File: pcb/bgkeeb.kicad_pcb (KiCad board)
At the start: 2 copper layers, 98.4 x 90.5 mm, 102 parts, among them J1 Pimoroni, SW1 SW_Push, SW11 SW_Push, SW12 SW_Push, SW13 SW_Push, SW14 SW_Push, SW15 SW_Push, SW2 SW_Push, SW21 SW_Push, SW22 SW_Push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

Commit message: updated TRRS order
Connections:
- U3 pad 1: Net-(U3-Pad1) -> GND
- U3 pad 2: data -> GND
- U3 pad 3: GND -> data
- U4 pad 1: Net-(U4-Pad1) -> GND
- U4 pad 2: data -> GND
- U4 pad 3: GND -> data
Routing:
- net GND: track 626.4 -> 632.7 mm, vias 57 -> 58
- net data: track 57.3 -> 63.5 mm, vias 2 -> 4

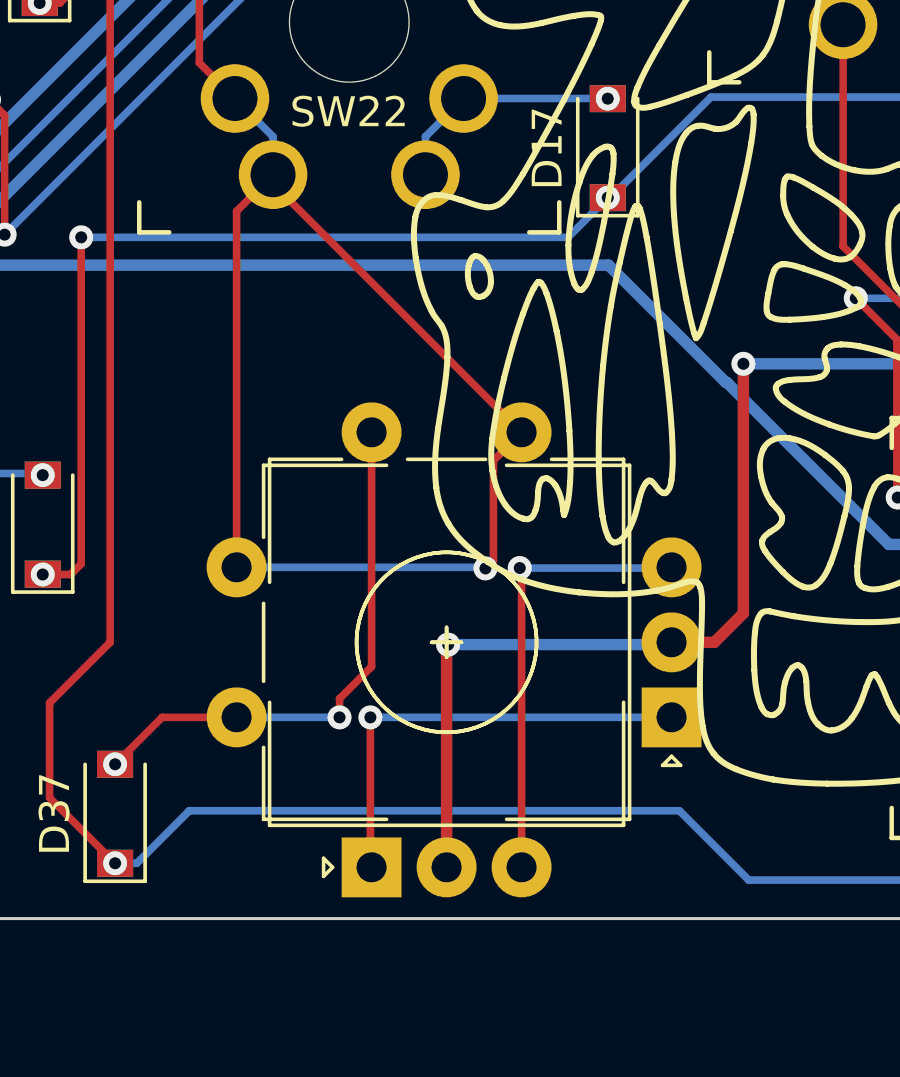
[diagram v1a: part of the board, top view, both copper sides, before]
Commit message: removed old gerber files, fixed rotary encoder on the back
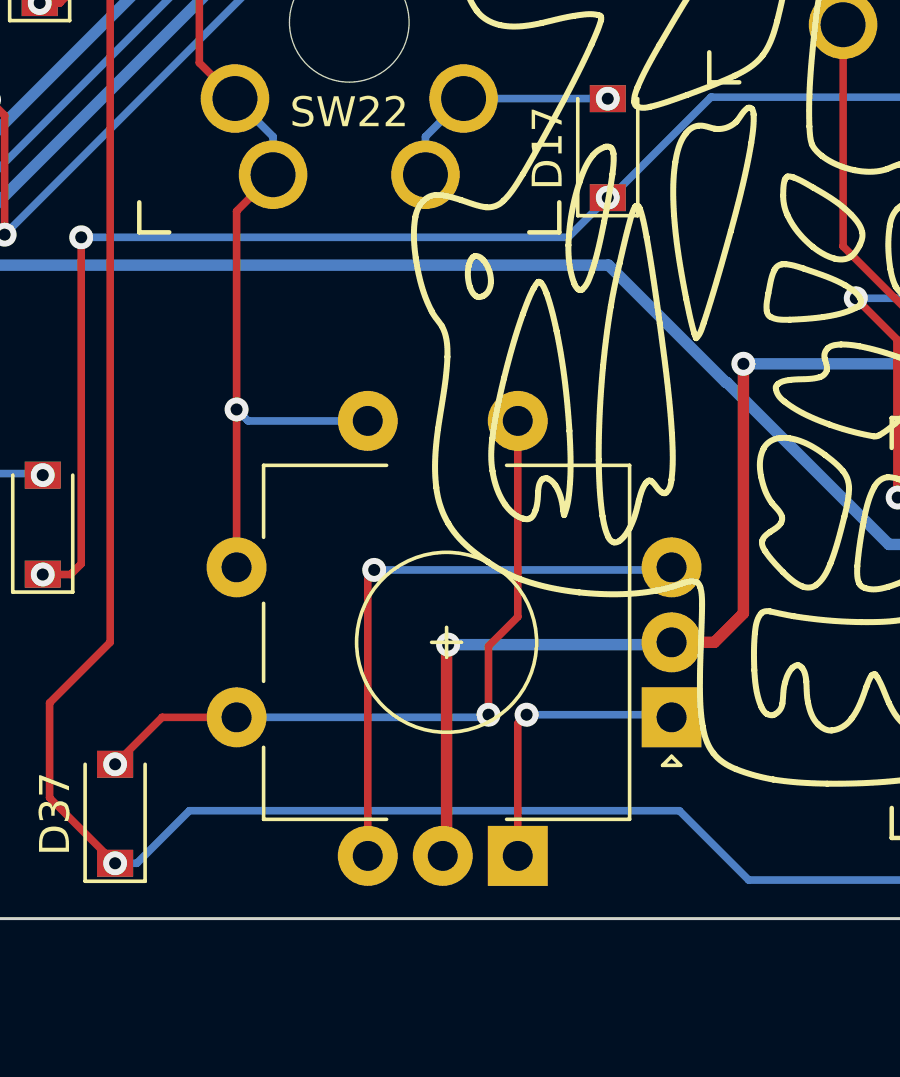
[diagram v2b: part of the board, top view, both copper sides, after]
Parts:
- SW7: moved to B.Cu
- moved SW7 0.40 mm to (83.1, 103.8)
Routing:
- net col1: track 99.6 -> 79.0 mm
- net ENC1A: track 15.1 -> 9.70 mm
- net Net-(D37-Pad2): track 18.1 -> 23.3 mm
- net ENC1B: track 15.1 -> 19.6 mm

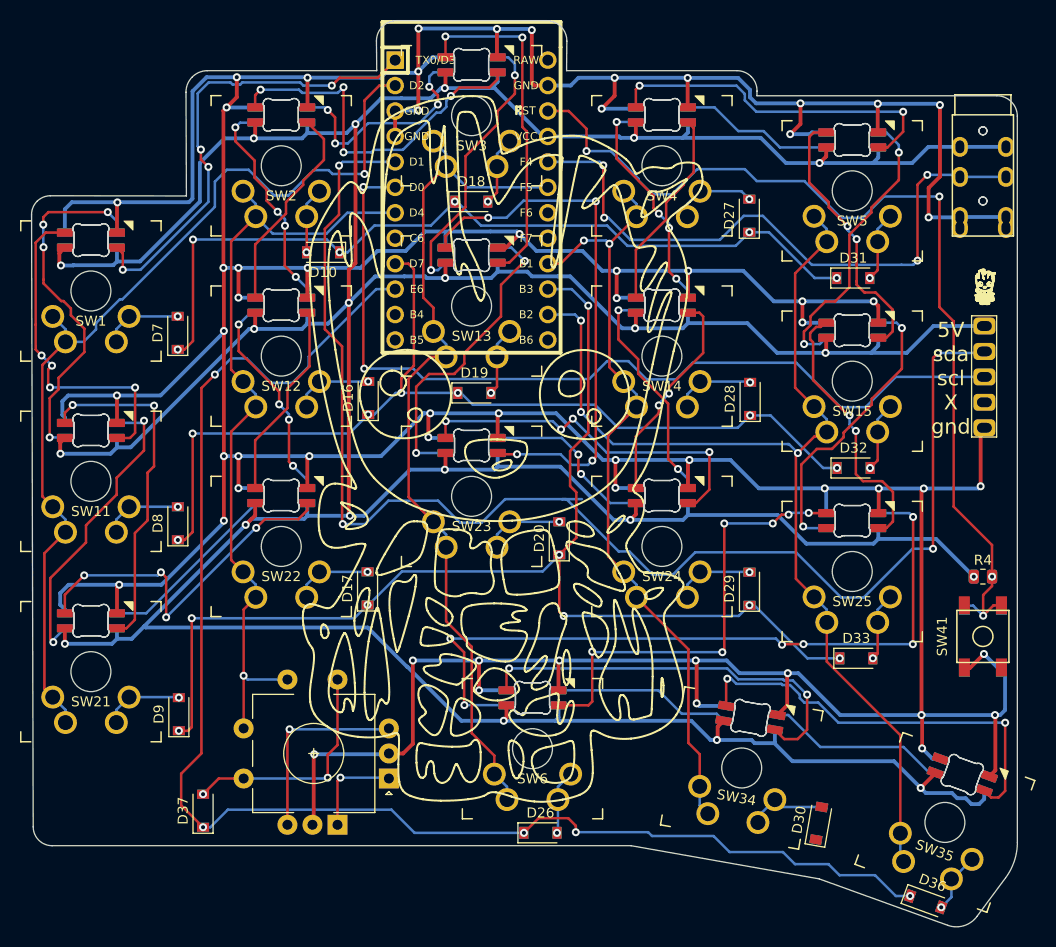
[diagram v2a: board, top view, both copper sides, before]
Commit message: Updated to add mounting holes
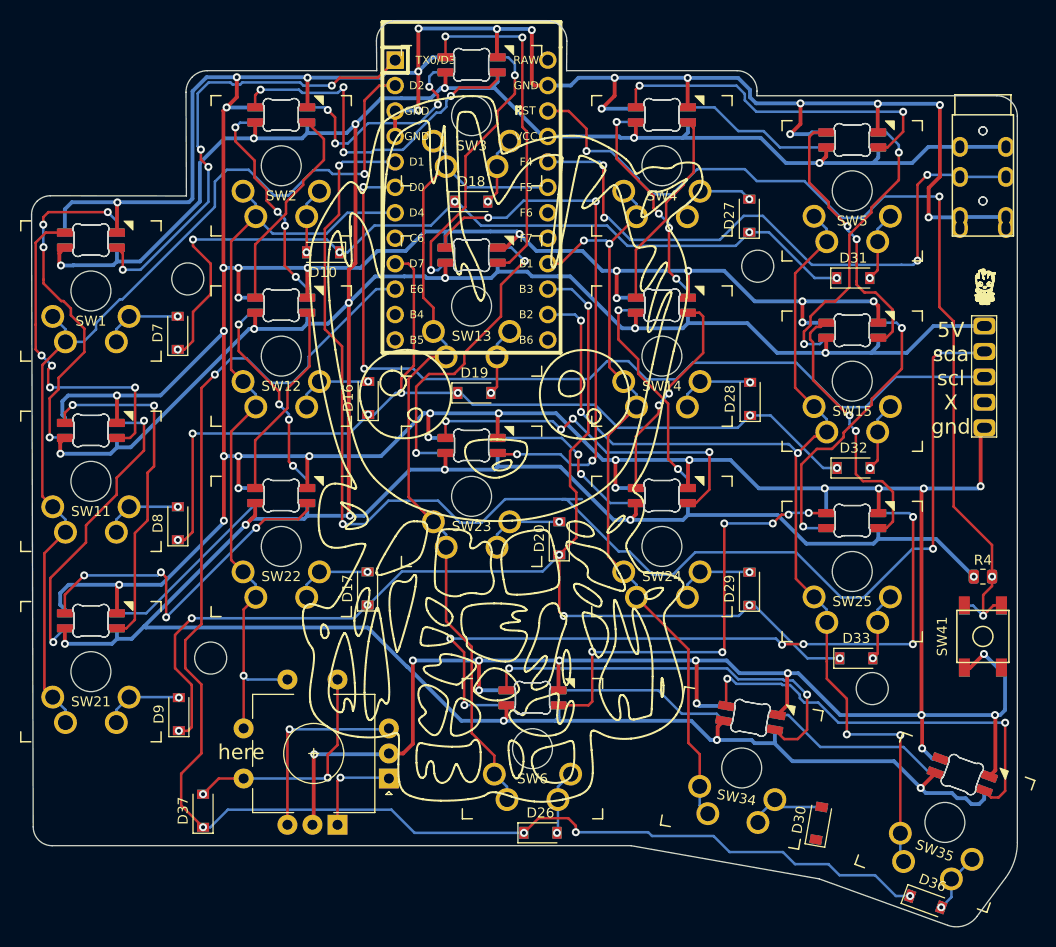
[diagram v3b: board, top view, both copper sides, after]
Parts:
- added ?: MountingHole_3.2mm_M3, MountingHole:MountingHole_3.2mm_M3, F.Cu at (73.0, 94.7)
- added ?: MountingHole_3.2mm_M3, MountingHole:MountingHole_3.2mm_M3, F.Cu at (70.7, 56.8)
- added ?: MountingHole_3.2mm_M3, MountingHole:MountingHole_3.2mm_M3, F.Cu at (127.6, 55.6)
- added ?: MountingHole_3.2mm_M3, MountingHole:MountingHole_3.2mm_M3, F.Cu at (139.0, 97.7)
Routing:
- net col4: track 109.8 -> 112.9 mm, vias 3 -> 5
- net row0: track 83.2 -> 84.6 mm
- net row2: track 119.4 -> 120.8 mm
- net row3: track 148.1 -> 149.4 mm
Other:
- board text added: "here"

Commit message: aux jack wasn't wired, no functional impact, just got DRC errors
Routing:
- net GND: track 632.7 -> 634.9 mm

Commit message: fixed a lot of things
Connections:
- U1 pad 18: Net-(U1-Pad18) -> row0
- U1 pad 2: col0 -> data
- U1 pad 20: data -> col0
- U1 pad 24: row0 -> Net-(U1-Pad24)
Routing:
- net ENC1A: track 9.70 -> 63.0 mm
- net ENC1B: track 19.6 -> 60.7 mm, vias 1 -> 3
- net data: track 63.5 -> 85.1 mm, vias 4 -> 5
- net led: track 46.6 -> 58.5 mm, vias 4 -> 5
- net col0: track 96.8 -> 107.9 mm, vias 1 -> 2
- net row3: track 149.4 -> 152.1 mm, vias 5 -> 6
- net +5V: track 500.7 -> 502.5 mm, vias 21 -> 22
- net row0: track 84.6 -> 85.7 mm
- net Net-(D30-Pad2): vias 0 -> 1

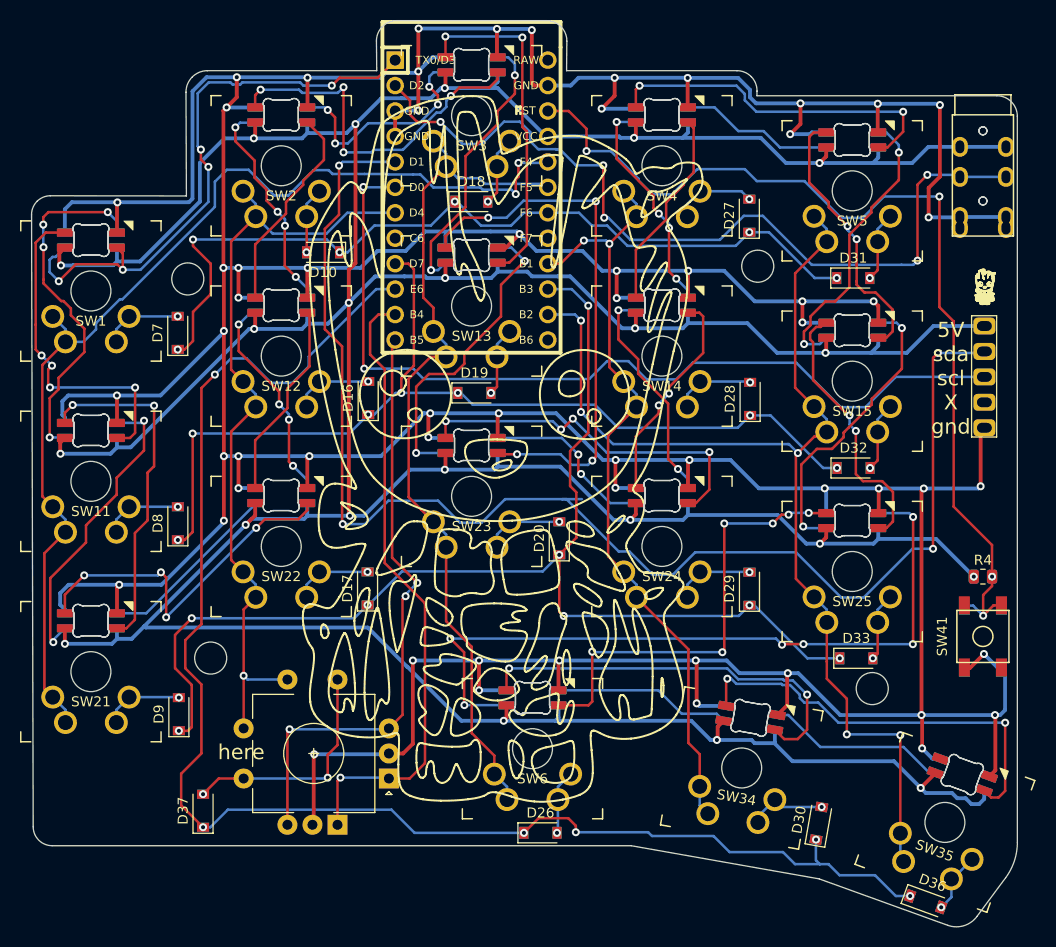
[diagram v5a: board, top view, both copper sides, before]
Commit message: v2 fixes the diode direction being flipped on the reverse side of the board
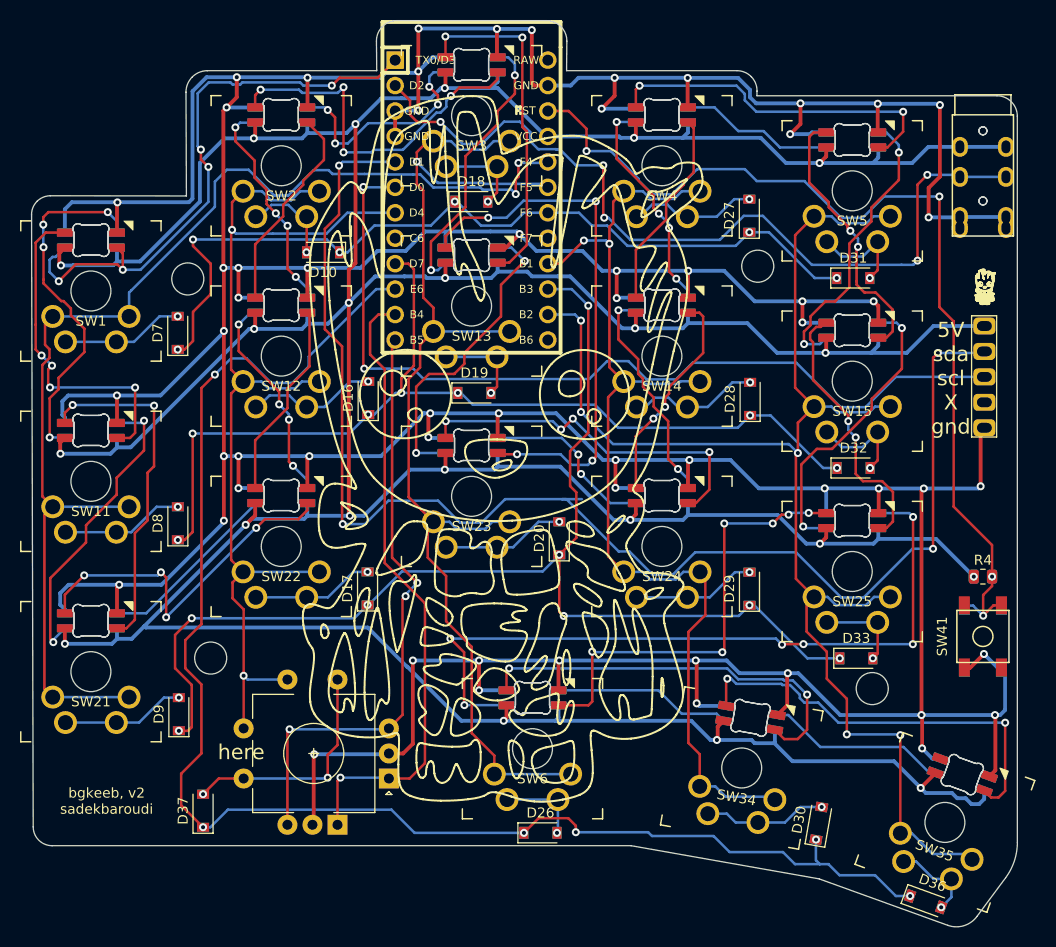
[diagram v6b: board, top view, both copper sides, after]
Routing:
- net col2: track 85.7 -> 115.8 mm, vias 0 -> 1
- net col4: track 112.9 -> 140.8 mm
- net col3: track 77.4 -> 102.9 mm
- net col1: track 79.0 -> 102.5 mm, vias 1 -> 2
- net col0: track 107.9 -> 119.6 mm
- net Net-(D12-Pad2): track 7.94 -> 13.2 mm
- net Net-(D14-Pad2): track 8.10 -> 13.2 mm
- net Net-(D27-Pad2): track 8.31 -> 13.0 mm
- net Net-(D17-Pad2): track 7.87 -> 12.5 mm
- net Net-(D30-Pad2): track 7.96 -> 12.4 mm
- net Net-(D21-Pad2): track 8.06 -> 12.4 mm
- net Net-(D24-Pad2): track 8.01 -> 12.4 mm
- net Net-(D1-Pad2): track 7.93 -> 12.3 mm
- net Net-(D11-Pad2): track 7.94 -> 12.3 mm
- net Net-(D20-Pad2): track 8.01 -> 12.3 mm
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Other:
- board text added: "bgkeeb, v2 sadekbaroudi"
